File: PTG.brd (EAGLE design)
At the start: 105.4 x 82.5 mm, 86 parts, among them IC1 TPS62120, IC2 PIC32MK1024MCF064-I_PT, IC3 LT1762EMS8-5PBF, IC4 TPS561208DDCR, IC5 LT1762EMS8-5PBF, J1 STX-3100-5N, J2 RCJ-01X_PHONO_SINGLE, U4 PCM1748E/2K, X1 22-23-2041

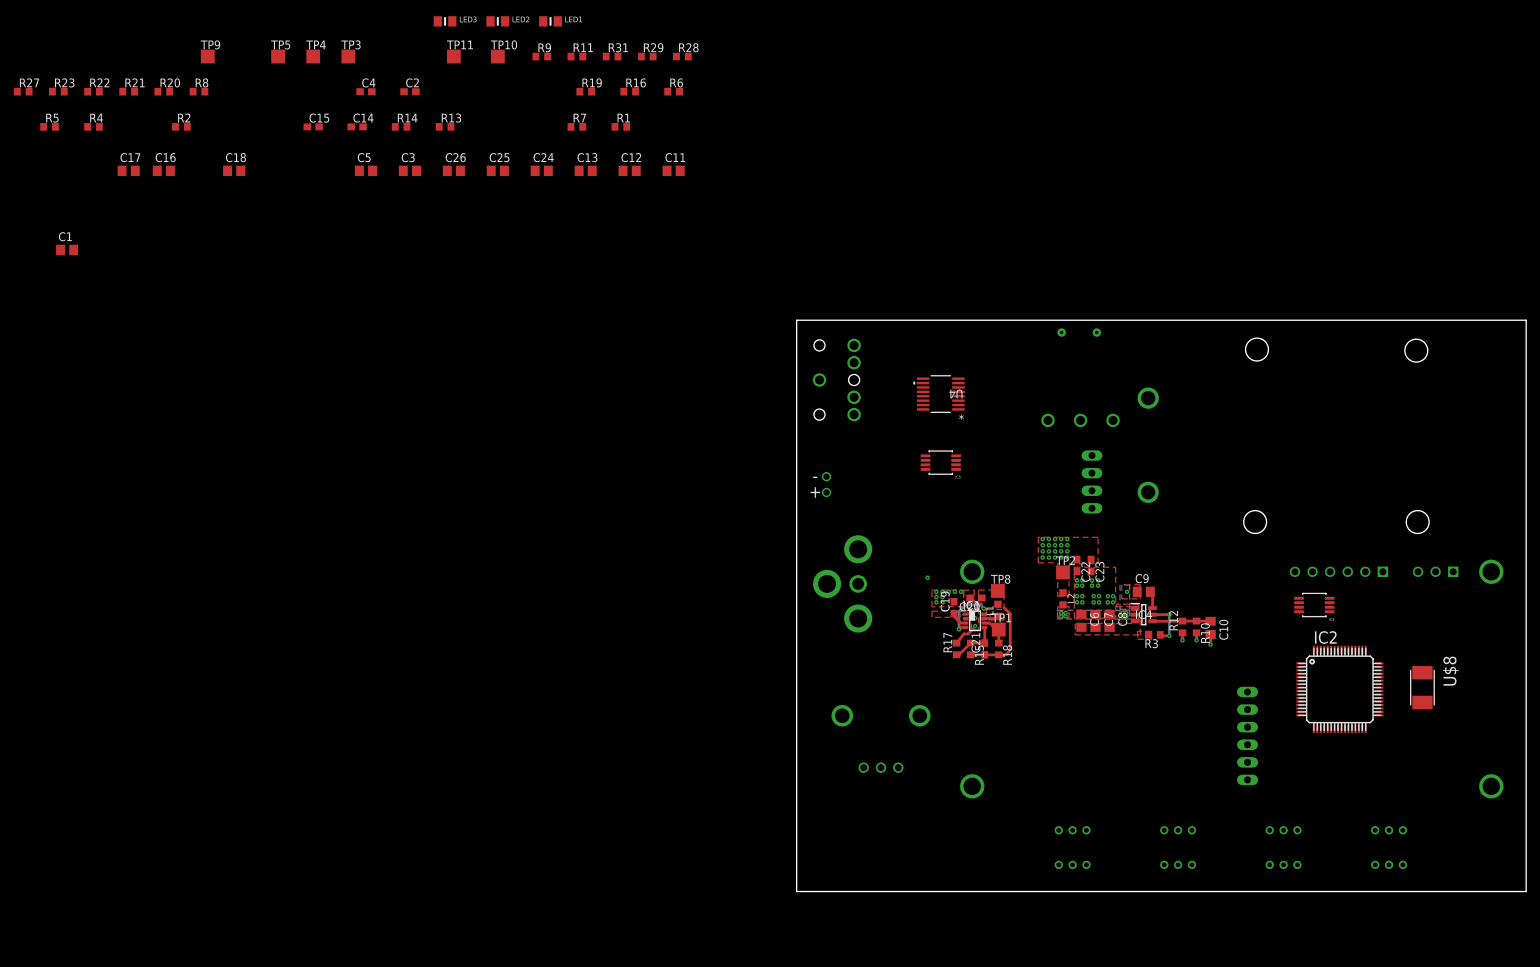
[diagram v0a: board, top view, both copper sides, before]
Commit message: Minor changes to schematic, added LDO traces, added DAC traces, added power traces
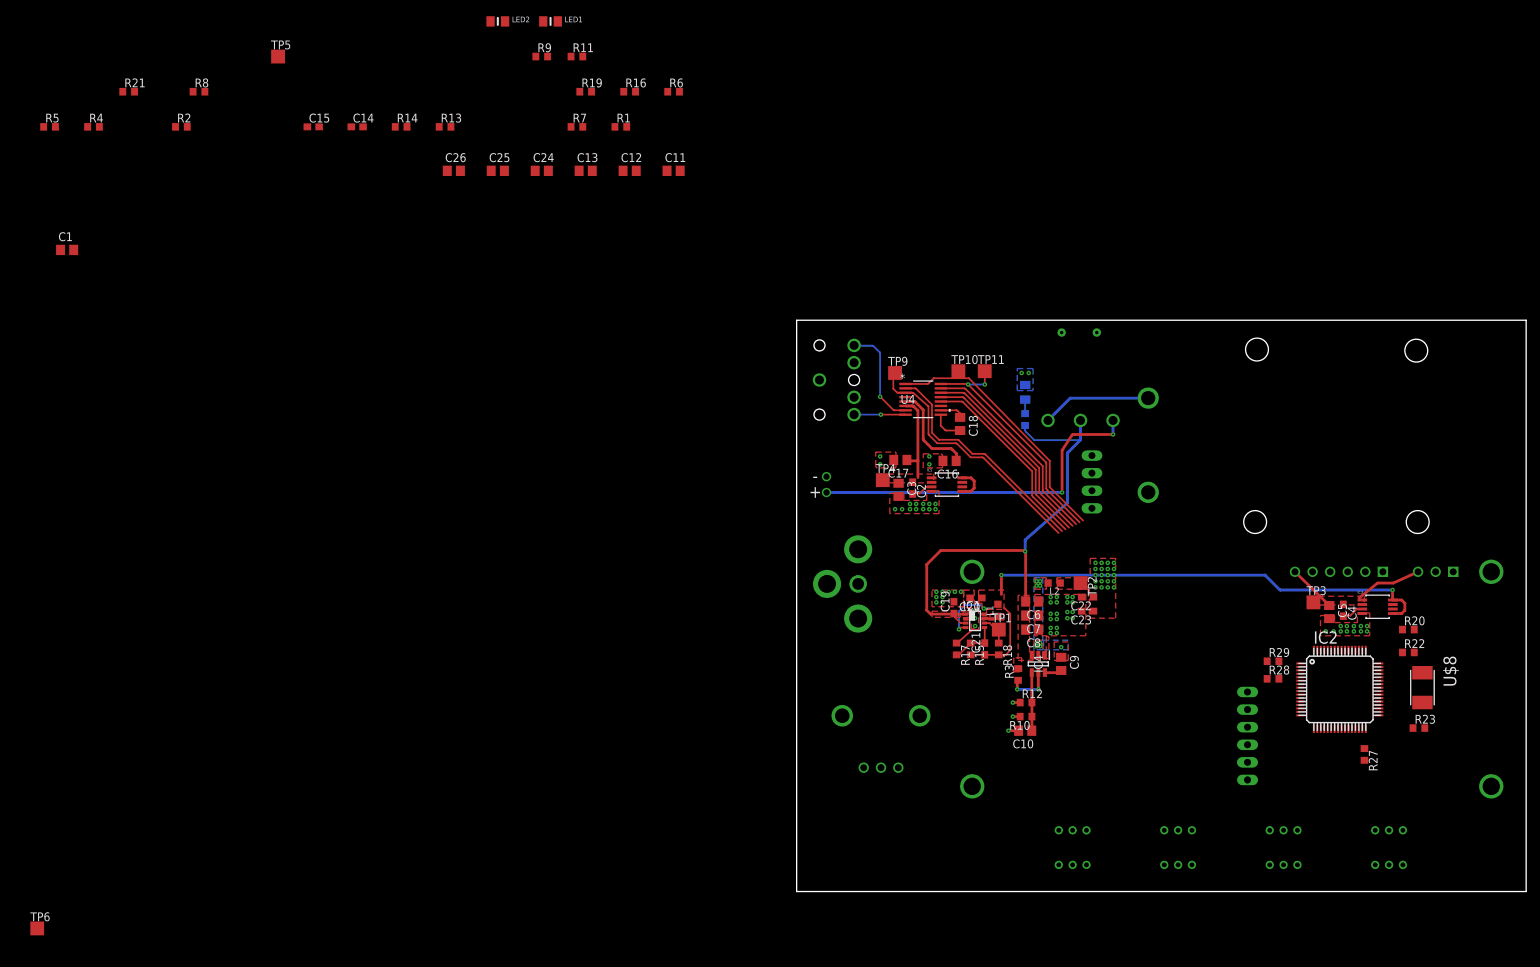
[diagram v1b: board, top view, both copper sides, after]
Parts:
- removed TP8: TPTP20SQ, testpad:TP20SQ
- added TP6: TPTP20SQ, testpad:TP20SQ
- R1: value 1.00K -> 1.00k
- R10: value 3.09K -> 3.09k
- R12, R13, R14, R7: value 10.0K -> 10.0k
- R15: value 562K -> 562k
- R17, R18: value 100K -> 100k
- moved R23 217.0 mm to (89.9, 23.6)
- moved R27 216.2 mm to (82.0, 19.8), turned to 270 degrees
- moved R22 206.5 mm to (88.4, 34.5)
- moved R20 195.9 mm to (88.4, 37.8)
- moved TP3 160.2 mm to (74.7, 41.8)
- moved C4 159.9 mm to (79.0, 40.6), turned to 270 degrees
- moved C5 153.1 mm to (77.0, 40.4), turned to 270 degrees
- moved R29 125.7 mm to (68.8, 33.3)
- moved R28 124.0 mm to (68.8, 30.7)
- moved C16 121.0 mm to (22.1, 62.2), turned to 180 degrees
- moved C17 119.1 mm to (15.0, 62.4), turned to 180 degrees
- moved C18 111.1 mm to (23.6, 67.6), turned to 270 degrees
- moved TP9 109.3 mm to (14.2, 74.9)
- moved TP4 102.6 mm to (12.4, 59.4)
- moved LED3 99.5 mm to (33.0, 72.1), flipped to the bottom, turned to 270 degrees
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- renumbered U$2 to BATT_HOLDER, U$3 to ROCKER_SW
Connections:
- net ADD_TEST_PAD renamed PWRGOOD
- net N$1 renamed SW-B
- net PWR_PINS renamed PWR_PIN
- net 5V_I/O: now also TP6.TP; no longer TP8.TP
- net GND: now also R17.1; no longer R17.2
- net N$11: now also IC2.30, R11.1; no longer LED2.2, R9.1
- net N$12: now also R11.2; no longer R11.1
- net N$15: now also LED2.2, R9.2; no longer IC2.30, R11.2
- net N$17: now also R9.1; no longer R9.2
- net N$8: now also R17.2; no longer R17.1
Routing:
- net 5V_I/O: track 20.4 -> 91.8 mm, vias 2 -> 4
- net SUPPLY: track 1.92 -> 68.6 mm, vias 0 -> 1
- net PWR_PIN: track 0.00 -> 50.7 mm, vias 1 -> 3
- net DAC_BCK: track 0.00 -> 37.9 mm
- net DAC_LRCK: track 0.00 -> 37.1 mm
- net SYS_CLK: track 0.00 -> 34.9 mm, vias 0 -> 2
- net DAC_DATA: track 0.00 -> 33.5 mm
- net !DAC_CS: track 0.00 -> 29.7 mm
- net DAC_SPI_CLK: track 0.00 -> 29.1 mm
- net DAC_SPI_DATA: track 0.00 -> 28.4 mm
- net DAC_ZEROL: track 0.00 -> 27.7 mm
- net VOUT_LCD: track 0.00 -> 16.6 mm
- net SW-B: track 0.00 -> 15.8 mm
- net SIGNAL_L: track 0.00 -> 15.0 mm, vias 0 -> 1
- net +3V3: track 3.41 -> 17.4 mm
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- added copper zone on layer 1, net +5_DAC
- added copper zone on layer 16, net GND
- added copper zone on layer 1, net VOUT_LCD

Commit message: re-routed DAC data traces, added traces to all components, just connecting data traces left
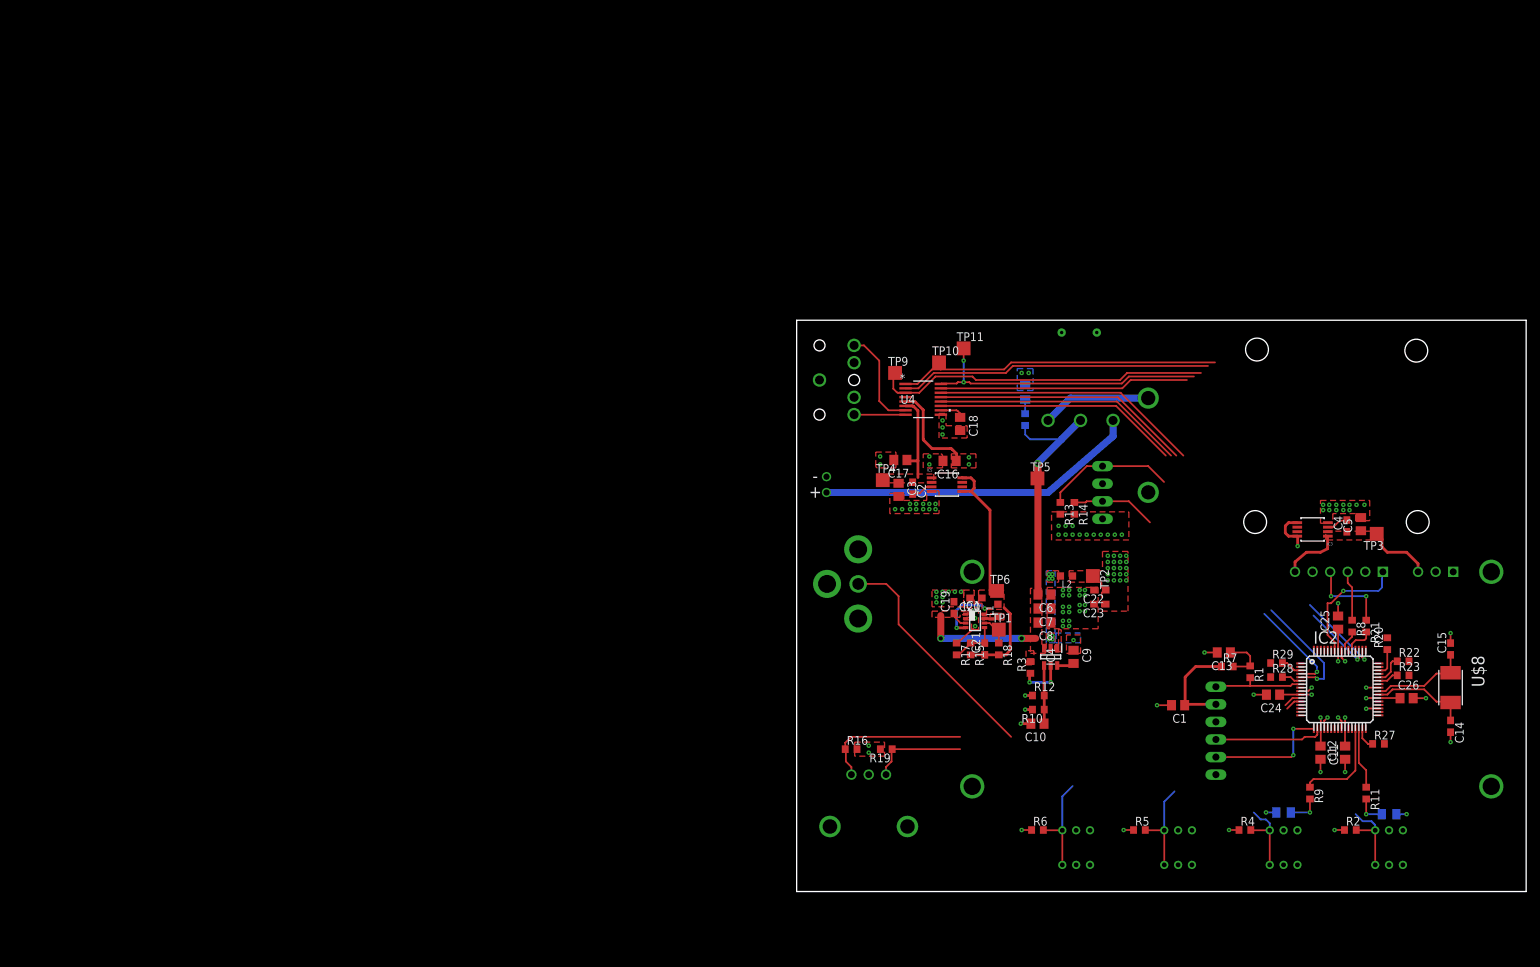
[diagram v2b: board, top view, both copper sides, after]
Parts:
- moved R2 197.1 mm to (80.0, 8.89)
- moved R4 194.9 mm to (64.8, 8.89)
- moved R21 194.8 mm to (82.3, 38.4), turned to 270 degrees
- moved R5 187.4 mm to (49.5, 8.89)
- moved R8 183.6 mm to (80.3, 38.4), turned to 270 degrees
- moved C15 180.8 mm to (94.5, 35.1), turned to 90 degrees
- moved C14 180.2 mm to (94.5, 23.9), turned to 270 degrees
- moved C1 173.5 mm to (55.1, 26.9), turned to 180 degrees
- moved LED1 166.7 mm to (85.6, 11.2), flipped to the bottom
- moved LED2 161.1 mm to (70.4, 11.4), flipped to the bottom, turned to 180 degrees
- moved C26 157.3 mm to (88.1, 27.9)
- moved R11 156.0 mm to (82.3, 14.2), turned to 270 degrees
- moved R9 153.8 mm to (74.2, 14.2), turned to 270 degrees
- moved TP6 147.0 mm to (29.0, 43.4)
- moved C25 137.8 mm to (78.2, 38.9), turned to 90 degrees
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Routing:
- net DAC_ZEROH: track 0.00 -> 52.0 mm, vias 0 -> 1
- net 5V_I/O: track 91.8 -> 49.1 mm, vias 4 -> 3
- net +3V3: track 17.4 -> 56.4 mm, vias 22 -> 45
- net GND: track 4.26 -> 38.3 mm, vias 64 -> 84
- net TRIGGER: track 0.00 -> 33.6 mm
- net UART-RX: track 0.00 -> 31.6 mm, vias 0 -> 1
- net ENC_A: track 0.00 -> 24.3 mm
- net DAC_ZEROL: track 27.7 -> 50.6 mm, vias 0 -> 1
- net UART-TX: track 0.00 -> 22.7 mm, vias 0 -> 1
- net DIS_!CS: track 0.00 -> 18.3 mm, vias 0 -> 1
- net N$16: track 0.00 -> 18.1 mm, vias 0 -> 2
- net ENC_B: track 0.00 -> 16.5 mm
- net N$25: track 0.00 -> 15.8 mm
- net SUPPLY: track 68.6 -> 53.6 mm, vias 1 -> 3
- net BUTTON4: track 0.00 -> 14.8 mm
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- added copper zone on layer 1, net AGND

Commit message: finished all traces except 2 I have questions on
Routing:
- net DAC_DATA: track 45.0 -> 129.1 mm, vias 0 -> 2
- net !DAC_CS: track 36.0 -> 115.4 mm, vias 0 -> 2
- net DAC_SPI_DATA: track 37.5 -> 115.5 mm
- net DAC_SPI_CLK: track 38.8 -> 116.6 mm, vias 0 -> 2
- net SYS_CLK: track 42.1 -> 106.5 mm, vias 2 -> 4
- net ENC_B: track 16.5 -> 76.9 mm, vias 0 -> 2
- net ENC_A: track 24.3 -> 84.7 mm, vias 0 -> 2
- net DAC_BCK: track 47.1 -> 100.9 mm, vias 0 -> 2
- net DAC_LRCK: track 48.7 -> 100.6 mm, vias 0 -> 2
- net BUTTON4: track 14.8 -> 65.8 mm, vias 0 -> 1
- net 5V_I/O: track 49.1 -> 93.6 mm, vias 3 -> 4
- net TRIGGER: track 33.6 -> 76.1 mm, vias 0 -> 1
- net BUTTON3: track 14.0 -> 51.2 mm
- net DAC_ZEROL: track 50.6 -> 83.2 mm, vias 1 -> 2
- net UART-RX: track 31.6 -> 63.5 mm, vias 1 -> 2
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
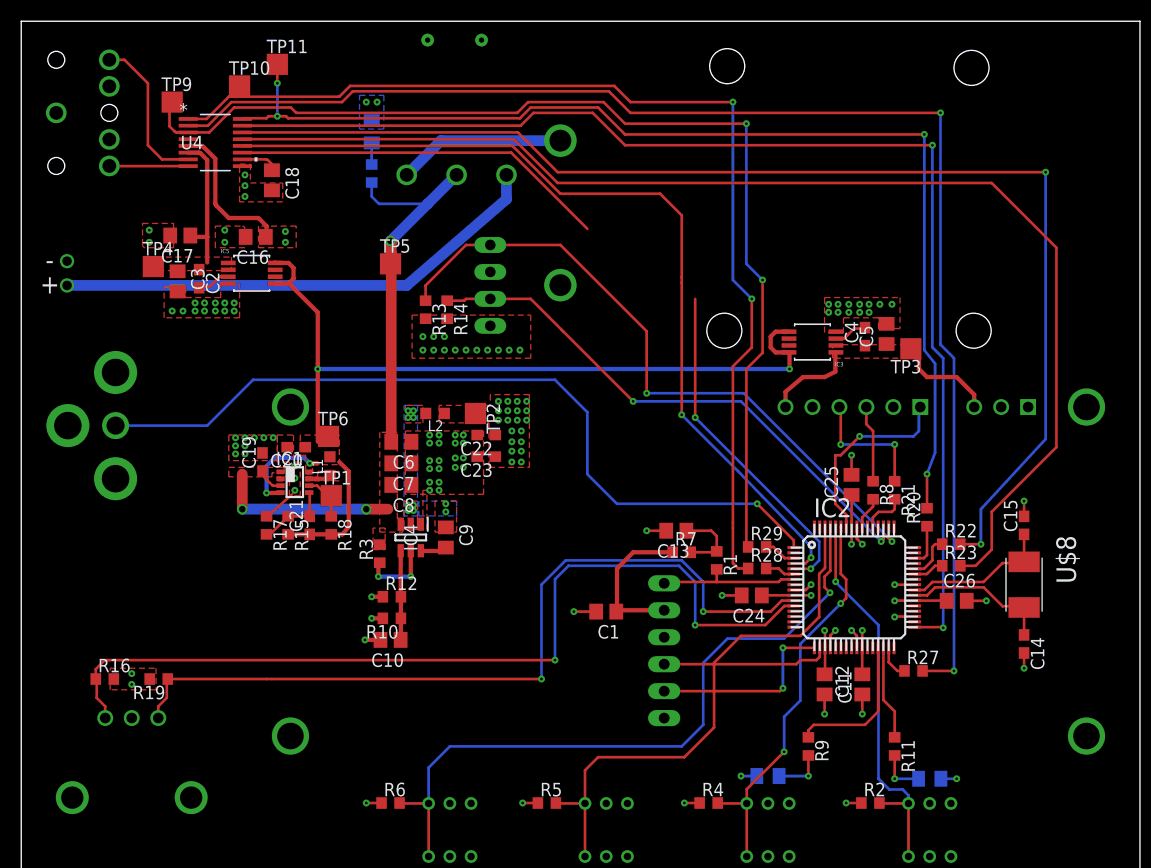
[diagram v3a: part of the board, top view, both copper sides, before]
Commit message: minor fixes, switched DAC_ZEROL / DAC ZEROH pins, need new test pad package
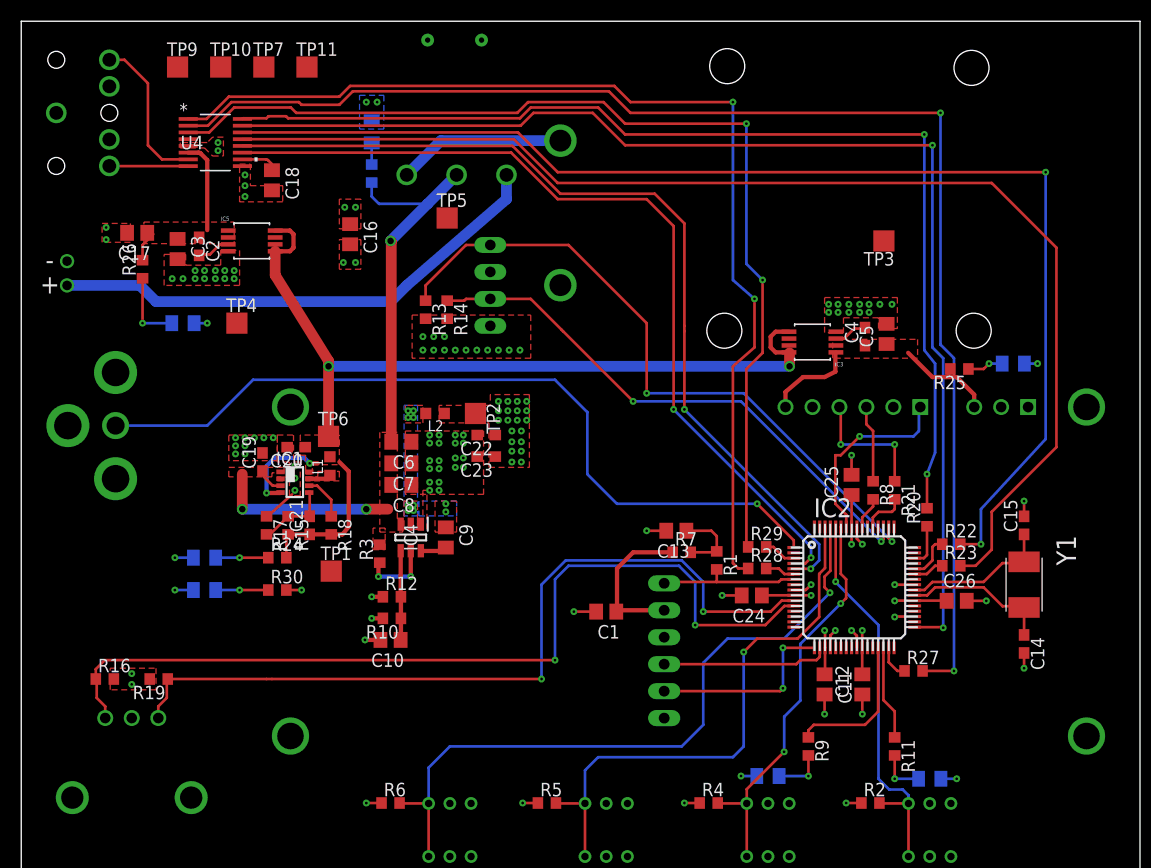
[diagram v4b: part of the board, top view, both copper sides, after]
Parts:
- added LED4, LED6, LED8, LED9: GREENLED, GreenLED:0805_10MGAP
- added R24, R25, R26, R30: (no value), resistor:R0603
- added TP7: TPTP20SQ, testpad:TP20SQ
- moved TP3 10.5 mm to (81.3, 61.8)
- moved TP4 9.51 mm to (20.3, 54.1)
- moved C16 8.89 mm to (31.0, 62.5), turned to 270 degrees
- moved TP1 7.11 mm to (29.2, 30.7)
- moved TP5 6.86 mm to (40.1, 64.0)
- moved C17 4.07 mm to (10.9, 62.6)
- moved TP9 3.34 mm to (14.7, 78.2)
- moved C2 3.05 mm to (16.8, 61.3)
- moved C3 3.05 mm to (14.7, 61.1)
- moved IC5 3.05 mm to (21.7, 61.8)
- moved TP11 2.81 mm to (26.9, 78.2)
- moved TP10 2.51 mm to (18.8, 78.2)
- renumbered U$1 to DIS1, U$8 to Y1
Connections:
- new net N$22: LED4.2, R24.1
- new net N$24: LED6.2, R25.1
- new net N$26: LED8.2, R26.1
- new net N$28: LED9.2, R30.1
- net +3V3: now also R30.2
- net +5_DAC: now also R26.2
- net 5V_I/O: now also R24.2
- net DAC_DATA: now also TP7.TP
- net DAC_ZEROH: now also IC2.4; no longer IC2.5
- net DAC_ZEROL: now also IC2.5; no longer IC2.4
- net GND: now also LED4.1, LED6.1, LED8.1, LED9.1
- net VOUT_LCD: now also R25.2
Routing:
- net DAC_ZEROH: track 67.7 -> 82.0 mm
- net +3V3: track 56.4 -> 43.8 mm, vias 45 -> 48
- net N$26: track 0.00 -> 6.99 mm, vias 0 -> 1
- net GND: track 38.3 -> 44.3 mm, vias 84 -> 88
- net N$28: track 0.00 -> 4.96 mm, vias 0 -> 1
- net N$22: track 0.00 -> 4.96 mm, vias 0 -> 1
- net SYS_CLK: track 106.5 -> 101.6 mm, vias 4 -> 2
- net DAC_LRCK: track 100.6 -> 96.2 mm
- net 5V_I/O: track 93.6 -> 97.6 mm
- net N$24: track 0.00 -> 3.39 mm, vias 0 -> 1
- net BUTTON3: track 51.2 -> 52.9 mm, vias 0 -> 1
- net +5_DAC: track 13.3 -> 11.8 mm
- net PWR_PIN: track 46.7 -> 48.0 mm
- net DAC_ZEROL: track 83.2 -> 84.4 mm
- net DAC_BCK: track 100.9 -> 100.2 mm
